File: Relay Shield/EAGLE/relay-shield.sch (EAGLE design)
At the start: 41 parts, among them IC1 MC33269T-5.0, J1 POWER_JACKSLT, T1 2N3904, T2 2N3904, T3 2N3904, T4 2N3904, U1 RELAYSONGLE, U2 RELAYSONGLE, U3 RELAYSONGLE, U4 RELAYSONGLE

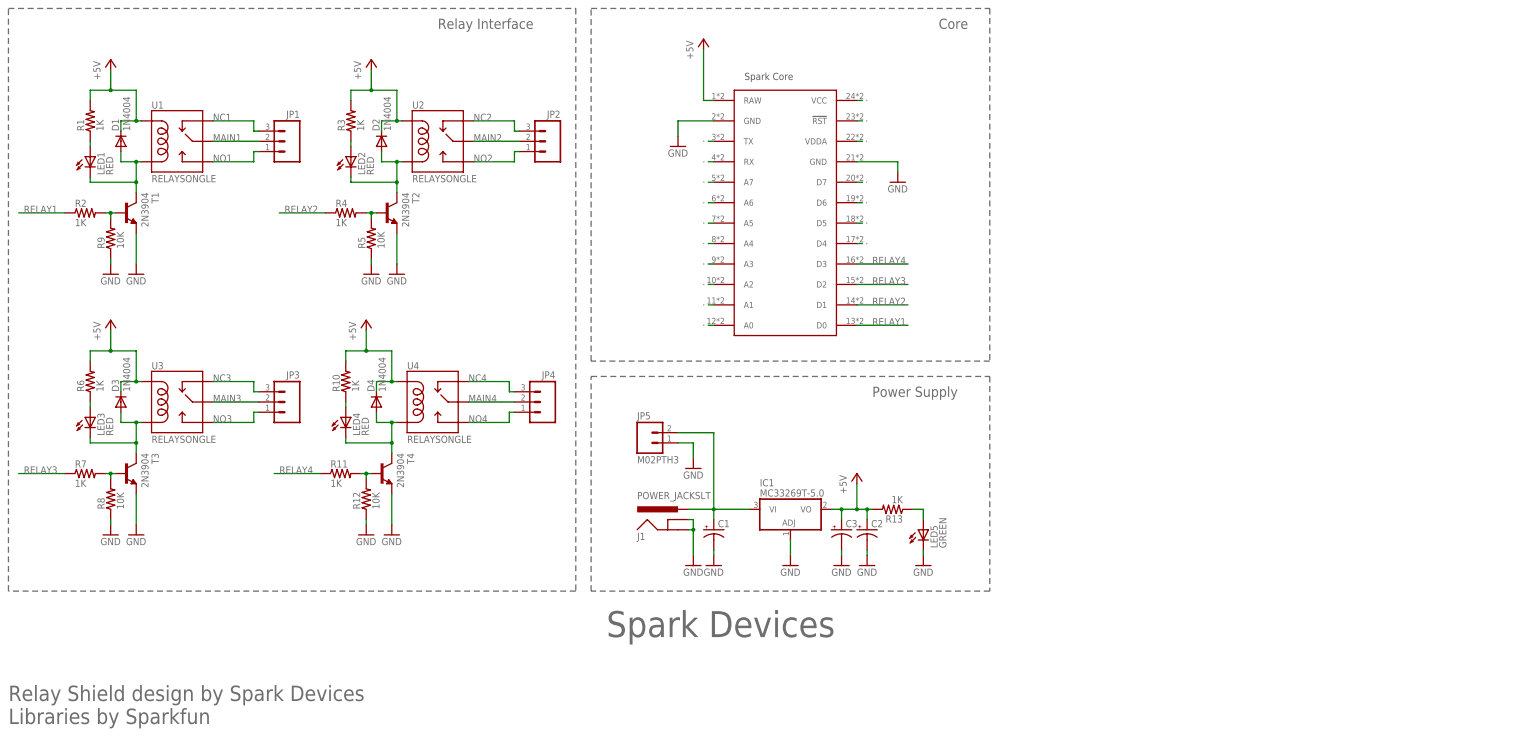
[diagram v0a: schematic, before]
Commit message: updated shield BOMs and boards
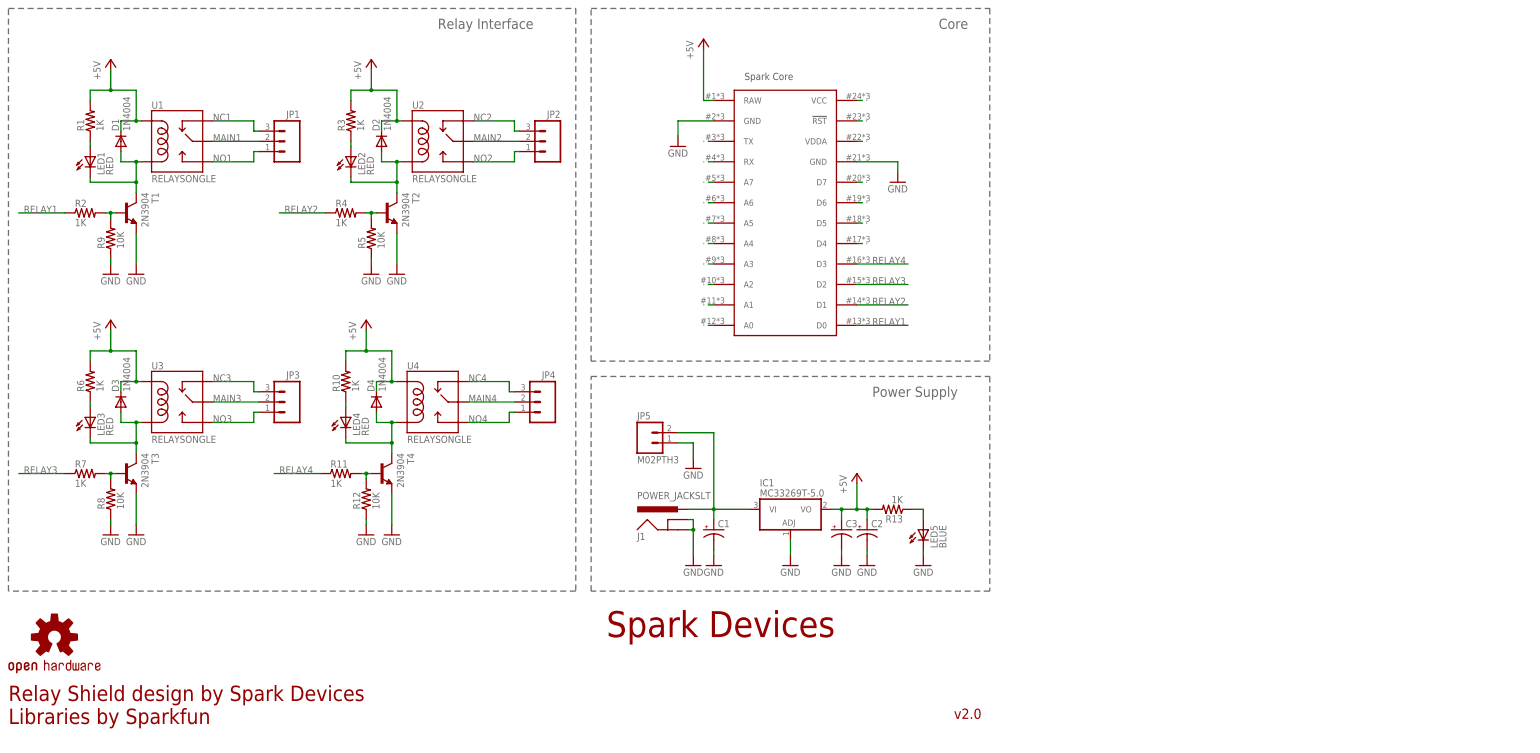
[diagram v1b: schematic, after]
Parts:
- added LOGO1: OSHW-LOGOM, Spark:OSHW-LOGOM
- J1: device SparkFun-Connectors:POWER_JACKSLT -> Spark:POWER_JACKSLT
- LED5: value GREEN -> BLUE
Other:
- note added: "v2.0"

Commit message: Major hoverhaul to the Relay Shield
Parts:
- removed C1, C2, C3: (no value), SparkFun-Passives:CAP_POLPTH1
- removed D3, D4: 1N4004, diode:1N4004
- removed IC1: MC33269T-5.0, linear:MC33269T-5.0
- removed T1, T2, T3, T4: 2N3904, transistor:2N3904
- added C4: 10nF, SparkFun-Capacitors:CAP0603-CAP
- added C5: 47uF, 25V, SparkFun-Capacitors:CAP_POLD
- added C6: 100uF, 10V, SparkFun-Capacitors:CAP_POLD
- added D5, D6, D7, D8: (no value), diode:DIODE-SOD123
- added L1: SDR1005-470KL, Spark:INDUCTOR-SPARKFUN
- added Q1, Q2, Q3, Q4: MPSA42, SparkFun-DiscreteSemi:TRANSISTOR_NPNMPSA42
- added U$2: LM2672, Spark:LM2672
- D1, D2: value 1N4004 -> B230; device diode:1N4004 -> adafruit:DIODESMA
- LED1, LED2, LED3, LED4, LED5: device SparkFun-LED:LED3MM -> SparkFun-LED:LED0603
- R1, R10, R11, R12, R13, R2, R3, R4, R5, R6, R7, R8, R9: device SparkFun-Passives:RESISTORAXIAL-0.3 -> SparkFun-Passives:RESISTOR0603-RES
- U1, U2, U3, U4: value RELAYSONGLE -> RELAYPANASONIC-JS; device Spark:RELAYSONGLE -> Spark:RELAYPANASONIC-JS
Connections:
- new net N$32: D2.A, J1.PWR, JP5.2
- new net N$33: C4.1, U$2.CB
- new net N$34: C4.2, D1.C, L1.1, U$2.VSW
- net +5V: now also C6.+, D5.C, D6.C, D7.C, D8.C, L1.2, U$2.FB; no longer C2.+, C3.+, D1.C, D2.C, D3.C, D4.C, IC1.VO
- net GND: now also C5.-, C6.-, D1.A, Q1.E, Q2.E, Q3.E, Q4.E, U$2.GND; no longer C1.-, C2.-, C3.-, IC1.ADJ, T1.E, T2.E, T3.E, T4.E
- net N$1: now also D5.A, Q1.C; no longer D1.A, T1.C
- net N$10: now also Q4.B; no longer T4.B
- net N$11: now also D8.A, Q4.C; no longer D4.A, T4.C
- net N$14: now also C5.+, D2.C, U$2.VIN; no longer C1.+, IC1.VI, J1.PWR, JP5.2
- net N$2: now also Q2.B; no longer T2.B
- net N$3: now also Q1.B; no longer T1.B
- net N$5: now also D6.A, Q2.C; no longer D2.A, T2.C
- net N$7: now also Q3.B; no longer T3.B
- net N$8: now also D7.A, Q3.C; no longer D3.A, T3.C
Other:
- moved on the sheet: J1, JP5, LED5, R13

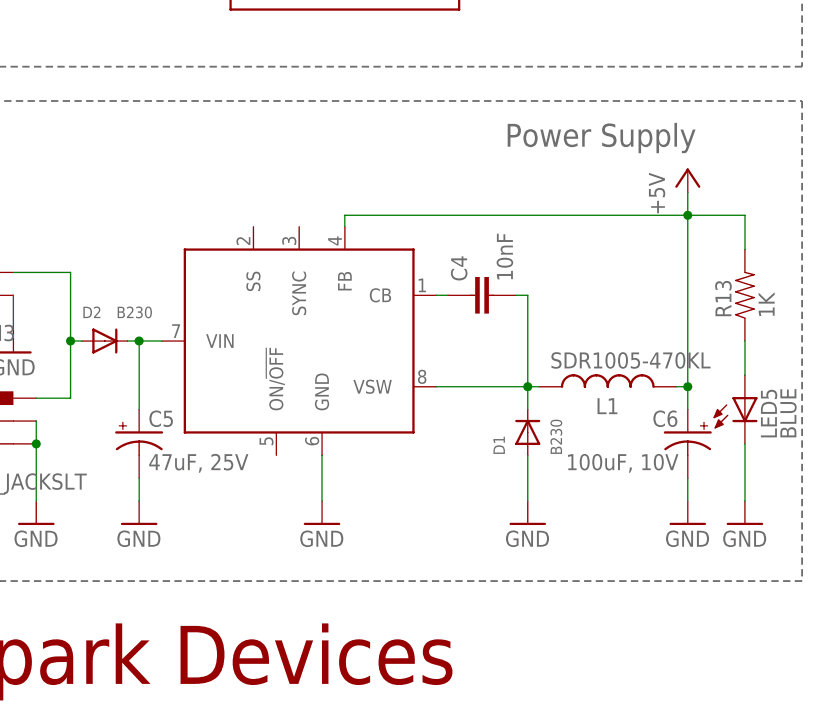
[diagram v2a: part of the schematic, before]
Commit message: changed the voltage regulator on the relay shield
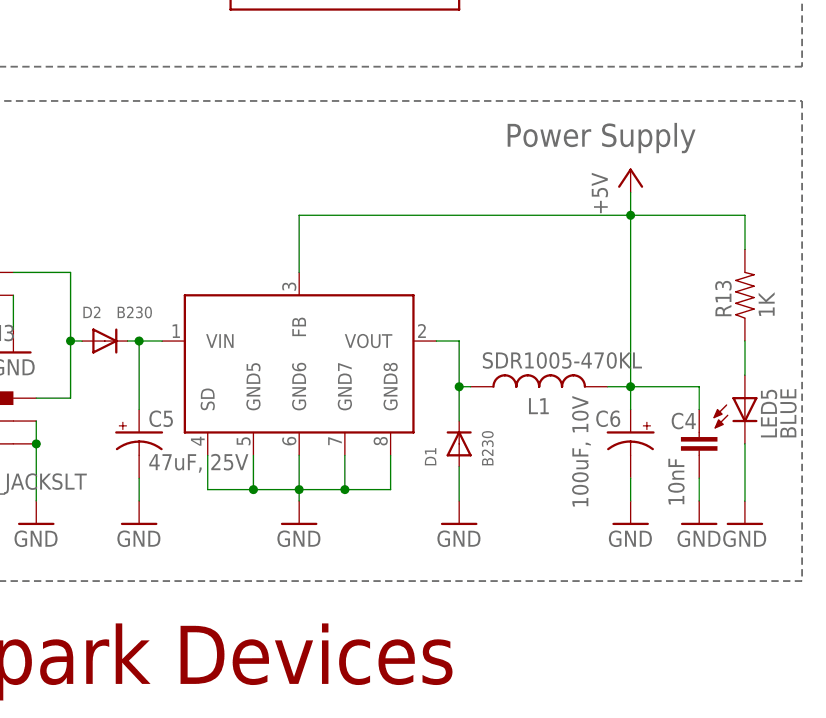
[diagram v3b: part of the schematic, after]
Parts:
- U$2: value LM2672 -> AP1509-50SG-13; device Spark:LM2672 -> Spark:AP1509-50SG-13
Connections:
- removed net N$33: C4.1, U$2.CB
- net +5V: now also C4.2
- net GND: now also C4.1, U$2.GND5, U$2.GND6, U$2.GND7, U$2.GND8, U$2.SD; no longer U$2.GND
- net N$34: now also U$2.VOUT; no longer C4.2, U$2.VSW
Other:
- moved on the sheet: C4, C6, D1, L1

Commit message: updated part designators as per to Sir William's request
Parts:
- renumbered U$1 to U5, U$2 to U6
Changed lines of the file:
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@@
 <setting verticaltext="up"/>
 </settings>
-<grid distance="0.05" unitdist="inch" unit="inch" style="lines" multiple="1" display="no" altdistance="0.01" altunitdist="inch" altunit="inch"/>
+<grid distance="0.1" unitdist="inch" unit="inch" style="lines" multiple="1" display="no" altdistance="0.01" altunitdist="inch" altunit="inch"/>
 <layers>
 <layer number="1" name="Top" color="4" fill="1" visible="no" active="no"/>
@@
 <part name="R1" library="SparkFun-Passives" deviceset="RESISTOR" device="0603-RES" value="1K"/>
 <part name="R2" library="SparkFun-Passives" deviceset="RESISTOR" device="0603-RES" value="1K"/>
-<part name="U$1" library="Spark" deviceset="SPARK_CORE" device=""/>
+<part name="U5" library="Spark" deviceset="SPARK_CORE" device=""/>
 <part name="FRAME1" library="frames" deviceset="LETTER_L" device=""/>
 <part name="R9" library="SparkFun-Passives" deviceset="RESISTOR" device="0603-RES" value="10K"/>
@@
 <part name="GND14" library="supply1" deviceset="GND" device=""/>
 <part name="GND17" library="supply1" deviceset="GND" device=""/>
-<part name="U$2" library="Spark" deviceset="AP1509-50SG-13" device=""/>
+<part name="U6" library="Spark" deviceset="AP1509-50SG-13" device=""/>
 <part name="GND18" library="supply1" deviceset="GND" device=""/>
 <part name="GND13" library="supply1" deviceset="GND" device=""/>
@@
 <attribute name="VALUE" x="19.05" y="128.778" size="1.778" layer="96"/>
 </instance>
-<instance part="U$1" gate="G$1" x="195.58" y="132.08"/>
+<instance part="U5" gate="G$1" x="195.58" y="132.08"/>
 <instance part="FRAME1" gate="G$1" x="0" y="0"/>
 <instance part="FRAME1" gate="G$2" x="147.32" y="0"/>
@@
 <instance part="GND14" gate="1" x="227.33" y="44.45"/>
 <instance part="GND17" gate="1" x="158.75" y="63.5"/>
-<instance part="U$2" gate="G$1" x="190.5" y="62.23"/>
+<instance part="U6" gate="G$1" x="190.5" y="62.23"/>
 <instance part="GND18" gate="1" x="234.95" y="44.45"/>
 <instance part="GND13" gate="1" x="190.5" y="44.45"/>
@@
 <wire x1="177.8" y1="154.94" x2="168.91" y2="154.94" width="0.1524" layer="91"/>
 <wire x1="168.91" y1="154.94" x2="168.91" y2="151.13" width="0.1524" layer="91"/>
-<pinref part="U$1" gate="G$1" pin="GND@2"/>
+<pinref part="U5" gate="G$1" pin="GND@2"/>
 </segment>
 <segment>
@@
 <wire x1="223.52" y1="142.24" x2="223.52" y2="144.78" width="0.1524" layer="91"/>
 <wire x1="223.52" y1="144.78" x2="213.36" y2="144.78" width="0.1524" layer="91"/>
-<pinref part="U$1" gate="G$1" pin="GND@21"/>
+<pinref part="U5" gate="G$1" pin="GND@21"/>
 </segment>
 <segment>
@@
 </segment>
 <segment>
-<pinref part="U$2" gate="G$1" pin="SD"/>
+<pinref part="U6" gate="G$1" pin="SD"/>
 <wire x1="180.34" y1="52.07" x2="180.34" y2="48.26" width="0.1524" layer="91"/>
 <wire x1="180.34" y1="48.26" x2="185.42" y2="48.26" width="0.1524" layer="91"/>
-<pinref part="U$2" gate="G$1" pin="GND8"/>
+<pinref part="U6" gate="G$1" pin="GND8"/>
 <wire x1="185.42" y1="48.26" x2="190.5" y2="48.26" width="0.1524" layer="91"/>
 <wire x1="190.5" y1="48.26" x2="195.58" y2="48.26" width="0.1524" layer="91"/>
 <wire x1="195.58" y1="48.26" x2="200.66" y2="48.26" width="0.1524" layer="91"/>
 <wire x1="200.66" y1="48.26" x2="200.66" y2="52.07" width="0.1524" layer="91"/>
-<pinref part="U$2" gate="G$1" pin="GND5"/>
+<pinref part="U6" gate="G$1" pin="GND5"/>
 <wire x1="185.42" y1="52.07" x2="185.42" y2="48.26" width="0.1524" layer="91"/>
 <junction x="185.42" y="48.26"/>
-<pinref part="U$2" gate="G$1" pin="GND6"/>
+<pinref part="U6" gate="G$1" pin="GND6"/>
 <wire x1="190.5" y1="52.07" x2="190.5" y2="48.26" width="0.1524" layer="91"/>
 <junction x="190.5" y="48.26"/>
-<pinref part="U$2" gate="G$1" pin="GND7"/>
+<pinref part="U6" gate="G$1" pin="GND7"/>
 <wire x1="195.58" y1="52.07" x2="195.58" y2="48.26" width="0.1524" layer="91"/>
 <junction x="195.58" y="48.26"/>
@@
 <segment>
 <wire x1="177.8" y1="160.02" x2="175.26" y2="160.02" width="0.1524" layer="91"/>
-<pinref part="U$1" gate="G$1" pin="RAW"/>
+<pinref part="U5" gate="G$1" pin="RAW"/>
 <pinref part="P+2" gate="1" pin="+5V"/>
 <wire x1="175.26" y1="172.72" x2="175.26" y2="160.02" width="0.1524" layer="91"/>
@@
 <wire x1="234.95" y1="57.15" x2="234.95" y2="59.69" width="0.1524" layer="91"/>
 <wire x1="234.95" y1="59.69" x2="227.33" y2="59.69" width="0.1524" layer="91"/>
-<pinref part="U$2" gate="G$1" pin="FB"/>
+<pinref part="U6" gate="G$1" pin="FB"/>
 </segment>
 </net>
@@
 </segment>
 <segment>
-<pinref part="U$1" gate="G$1" pin="D3"/>
+<pinref part="U5" gate="G$1" pin="D3"/>
 <wire x1="213.36" y1="119.38" x2="226.06" y2="119.38" width="0.1524" layer="91"/>
 <label x="217.17" y="119.38" size="1.778" layer="95"/>
@@
 </segment>
 <segment>
-<pinref part="U$1" gate="G$1" pin="D2"/>
+<pinref part="U5" gate="G$1" pin="D2"/>
 <wire x1="213.36" y1="114.3" x2="226.06" y2="114.3" width="0.1524" layer="91"/>
 <label x="217.17" y="114.3" size="1.778" layer="95"/>
@@
 </segment>
 <segment>
-<pinref part="U$1" gate="G$1" pin="D1"/>
+<pinref part="U5" gate="G$1" pin="D1"/>
 <wire x1="213.36" y1="109.22" x2="226.06" y2="109.22" width="0.1524" layer="91"/>
 <label x="217.17" y="109.22" size="1.778" layer="95"/>
@@
 </segment>
 <segment>
-<pinref part="U$1" gate="G$1" pin="D0"/>
+<pinref part="U5" gate="G$1" pin="D0"/>
 <wire x1="213.36" y1="104.14" x2="226.06" y2="104.14" width="0.1524" layer="91"/>
 <label x="217.17" y="104.14" size="1.778" layer="95"/>
@@
 <net name="N$13" class="0">
 <segment>
-<pinref part="U$1" gate="G$1" pin="D4"/>
+<pinref part="U5" gate="G$1" pin="D4"/>
 <wire x1="213.36" y1="124.46" x2="215.9" y2="124.46" width="0.1524" layer="91" style="dashdot"/>
 </segment>
@@
 <net name="N$15" class="0">
 <segment>
-<pinref part="U$1" gate="G$1" pin="D5"/>
+<pinref part="U5" gate="G$1" pin="D5"/>
 <wire x1="213.36" y1="129.54" x2="215.9" y2="129.54" width="0.1524" layer="91" style="dashdot"/>
 </segment>
@@
 <net name="N$17" class="0">
 <segment>
-<pinref part="U$1" gate="G$1" pin="D6"/>
+<pinref part="U5" gate="G$1" pin="D6"/>
 <wire x1="213.36" y1="134.62" x2="215.9" y2="134.62" width="0.1524" layer="91" style="dashdot"/>
 </segment>
@@
 <net name="N$18" class="0">
 <segment>
-<pinref part="U$1" gate="G$1" pin="D7"/>
+<pinref part="U5" gate="G$1" pin="D7"/>
 <wire x1="213.36" y1="139.7" x2="215.9" y2="139.7" width="0.1524" layer="91" style="dashdot"/>
 </segment>
@@
 <net name="N$19" class="0">
 <segment>
-<pinref part="U$1" gate="G$1" pin="VDDA"/>
+<pinref part="U5" gate="G$1" pin="VDDA"/>
 <wire x1="213.36" y1="149.86" x2="215.9" y2="149.86" width="0.1524" layer="91" style="dashdot"/>
 </segment>
@@
 <net name="N$20" class="0">
 <segment>
-<pinref part="U$1" gate="G$1" pin="!RST"/>
+<pinref part="U5" gate="G$1" pin="!RST"/>
 <wire x1="213.36" y1="154.94" x2="215.9" y2="154.94" width="0.1524" layer="91" style="dashdot"/>
 </segment>
@@
 <net name="N$21" class="0">
 <segment>
-<pinref part="U$1" gate="G$1" pin="VCC"/>
+<pinref part="U5" gate="G$1" pin="VCC"/>
 <wire x1="213.36" y1="160.02" x2="215.9" y2="160.02" width="0.1524" layer="91" style="dashdot"/>
 </segment>
@@
 <net name="N$22" class="0">
 <segment>
-<pinref part="U$1" gate="G$1" pin="A0"/>
+<pinref part="U5" gate="G$1" pin="A0"/>
 <wire x1="177.8" y1="104.14" x2="175.26" y2="104.14" width="0.1524" layer="91" style="dashdot"/>
 </segment>
@@
 <net name="N$23" class="0">
 <segment>
-<pinref part="U$1" gate="G$1" pin="A1"/>
+<pinref part="U5" gate="G$1" pin="A1"/>
 <wire x1="177.8" y1="109.22" x2="175.26" y2="109.22" width="0.1524" layer="91" style="dashdot"/>
 </segment>
@@
 <net name="N$24" class="0">
 <segment>
-<pinref part="U$1" gate="G$1" pin="A2"/>
+<pinref part="U5" gate="G$1" pin="A2"/>
 <wire x1="177.8" y1="114.3" x2="175.26" y2="114.3" width="0.1524" layer="91" style="dashdot"/>
 </segment>
@@
 <net name="N$25" class="0">
 <segment>
-<pinref part="U$1" gate="G$1" pin="A3"/>
+<pinref part="U5" gate="G$1" pin="A3"/>
 <wire x1="177.8" y1="119.38" x2="175.26" y2="119.38" width="0.1524" layer="91" style="dashdot"/>
 </segment>
@@
 <net name="N$26" class="0">
 <segment>
-<pinref part="U$1" gate="G$1" pin="A4"/>
+<pinref part="U5" gate="G$1" pin="A4"/>
 <wire x1="177.8" y1="124.46" x2="175.26" y2="124.46" width="0.1524" layer="91" style="dashdot"/>
 </segment>
@@
 <net name="N$27" class="0">
 <segment>
-<pinref part="U$1" gate="G$1" pin="A5"/>
+<pinref part="U5" gate="G$1" pin="A5"/>
 <wire x1="177.8" y1="129.54" x2="175.26" y2="129.54" width="0.1524" layer="91" style="dashdot"/>
 </segment>
@@
 <net name="N$28" class="0">
 <segment>
-<pinref part="U$1" gate="G$1" pin="A6"/>
+<pinref part="U5" gate="G$1" pin="A6"/>
 <wire x1="177.8" y1="134.62" x2="175.26" y2="134.62" width="0.1524" layer="91" style="dashdot"/>
 </segment>
@@
 <net name="N$29" class="0">
 <segment>
-<pinref part="U$1" gate="G$1" pin="A7"/>
+<pinref part="U5" gate="G$1" pin="A7"/>
 <wire x1="177.8" y1="139.7" x2="175.26" y2="139.7" width="0.1524" layer="91" style="dashdot"/>
 </segment>
@@
 <net name="N$30" class="0">
 <segment>
-<pinref part="U$1" gate="G$1" pin="RX"/>
+<pinref part="U5" gate="G$1" pin="RX"/>
 <wire x1="177.8" y1="144.78" x2="175.26" y2="144.78" width="0.1524" layer="91" style="dashdot"/>
 </segment>
@@
 <net name="N$31" class="0">
 <segment>
-<pinref part="U$1" gate="G$1" pin="TX"/>
+<pinref part="U5" gate="G$1" pin="TX"/>
 <wire x1="177.8" y1="149.86" x2="175.26" y2="149.86" width="0.1524" layer="91" style="dashdot"/>
 </segment>
@@
 <wire x1="172.72" y1="64.77" x2="171.45" y2="64.77" width="0.1524" layer="91"/>
 <junction x="172.72" y="64.77"/>
-<pinref part="U$2" gate="G$1" pin="VIN"/>
+<pinref part="U6" gate="G$1" pin="VIN"/>
 </segment>
 </net>
@@
 <pinref part="L1" gate="G$1" pin="1"/>
 <wire x1="209.55" y1="59.69" x2="208.28" y2="59.69" width="0.1524" layer="91"/>
-<pinref part="U$2" gate="G$1" pin="VOUT"/>
+<pinref part="U6" gate="G$1" pin="VOUT"/>
 <wire x1="208.28" y1="59.69" x2="208.28" y2="64.77" width="0.1524" layer="91"/>
 <wire x1="208.28" y1="64.77" x2="205.74" y2="64.77" width="0.1524" layer="91"/>

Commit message: added license info to all design files
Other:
- note added: "Reference Designs ARE PROVIDED "AS IS" AND "WITH ALL FAULTS. SPARK LABS, INC ("SPARK") DISCLAIMS ALL OTHER WARRANTIES, EXPRESS OR IMPLIED, REGARDING PRODUCTS OR THE REFERENCE DESIGNS, INCLUDING BUT NOT LIMITED TO, ANY IMPLIED WARRANTIES OF MERCHANTABILITY, FITNESS FOR A PARTICULAR PURPOSE, OR NON-INFRINGEMENT. Spark may make changes to specifications and product descriptions at any time, without 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"
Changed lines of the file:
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@@
 <setting verticaltext="up"/>
 </settings>
-<grid distance="0.1" unitdist="inch" unit="inch" style="lines" multiple="1" display="no" altdistance="0.01" altunitdist="inch" altunit="inch"/>
+<grid distance="0.1" unitdist="inch" unit="inch" style="lines" multiple="1" display="yes" altdistance="0.01" altunitdist="inch" altunit="inch"/>
 <layers>
 <layer number="1" name="Top" color="4" fill="1" visible="no" active="no"/>
@@
 Libraries by Sparkfun</text>
 <text x="237.49" y="6.35" size="2.54" layer="94">v2.0</text>
+<text x="259.08" y="5.08" size="1.778" layer="95">Reference Designs ARE PROVIDED "AS IS" AND "WITH ALL FAULTS. SPARK LABS, INC
+("SPARK") DISCLAIMS ALL OTHER WARRANTIES, EXPRESS OR IMPLIED, REGARDING
+PRODUCTS OR THE REFERENCE DESIGNS, INCLUDING BUT NOT LIMITED TO, ANY
+IMPLIED WARRANTIES OF MERCHANTABILITY, FITNESS FOR A PARTICULAR PURPOSE,
+OR NON-INFRINGEMENT.
+Spark may make changes to specifications and product descriptions at any
+time, without notice. The Customer must not rely on the absence or
+characteristics of any features or instructions marked "reserved" or
+"undefined." Spark reserves these for future definition and shall have
+no responsibility whatsoever for conflicts or incompatibilities arising
+from future changes to them. The product information on the Web Site or
+Materials is subject to change without notice. Do not finalize a design
+with this information.
+Spark is a registered trademark.</text>
+<wire x1="254" y1="0" x2="254" y2="48.26" width="0.2032" layer="94"/>
+<wire x1="254" y1="48.26" x2="381" y2="48.26" width="0.2032" layer="94"/>
+<wire x1="381" y1="48.26" x2="381" y2="0" width="0.2032" layer="94"/>
+<wire x1="381" y1="0" x2="254" y2="0" width="0.2032" layer="94"/>
 </plain>
 <instances>
